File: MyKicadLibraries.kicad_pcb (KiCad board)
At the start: 2 copper layers, 168.6 x 98.9 mm, 32 parts, among them J1 Conn_01x08, J10 RCJ-22, J11 DIN-5, J12 Mini-DIN-6, J13 USB_A, J2 Conn_01x08, J3 POGO Pins, J4 c8-inlet, J5 FTDI, J6 Micro_SD_Card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

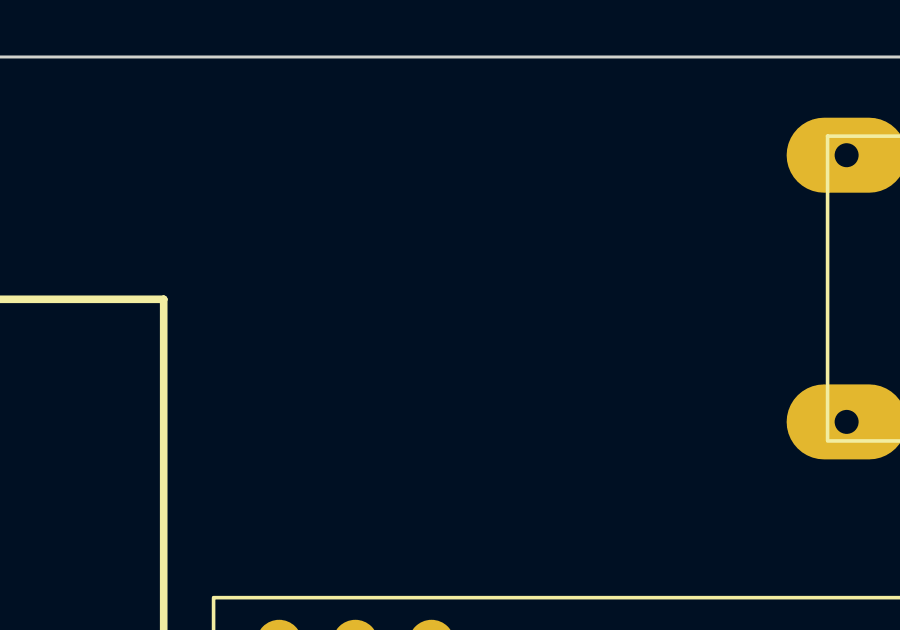
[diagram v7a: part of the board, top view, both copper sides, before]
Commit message: Add TCND5000 Library
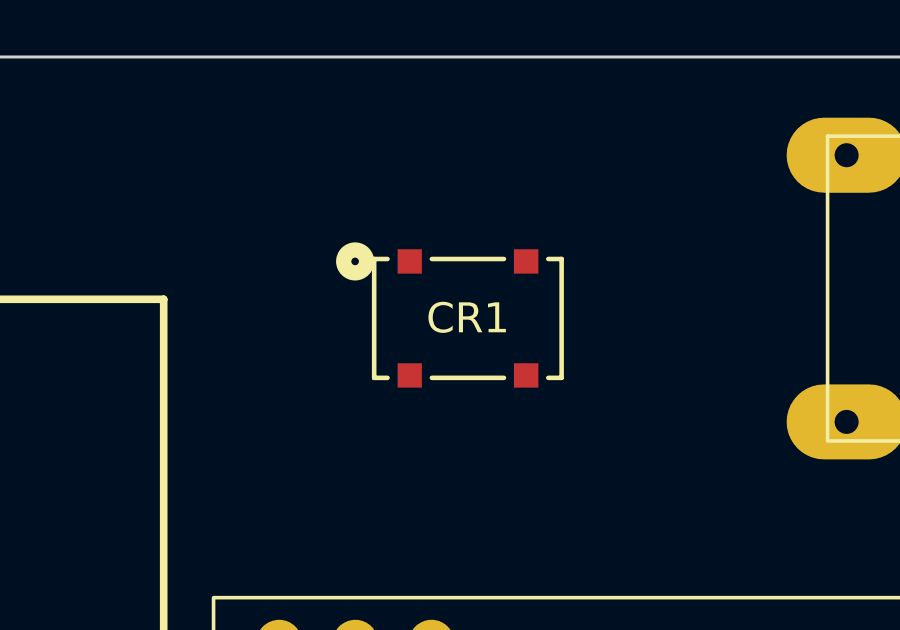
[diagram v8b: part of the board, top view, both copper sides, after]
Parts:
- added CR1: tcnd5000, tcnd5000:tcnd5000, F.Cu at (210.0, 33.0)
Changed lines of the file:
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@@
   (net 231 "unconnected-(J13-Pad3)")
   (net 232 "unconnected-(J13-Pad4)")
+  (net 233 "unconnected-(CR1-Pad1)")
+  (net 234 "unconnected-(CR1-Pad2)")
+  (net 235 "unconnected-(CR1-Pad4)")
+  (net 236 "unconnected-(CR1-Pad3)")
   (footprint "esp32-wemos-d1-mini:esp32-wemos-d1-mini" (layer "F.Cu")
     (at 118.11 138.43)
@@
     )
   )
+  (footprint "tcnd5000:tcnd5000" (layer "F.Cu")
+    (at 210 33)
+    (tags "tcnd5000 ")
+    (property "Sheetfile" "MyKicadLibraries.kicad_sch")
+    (property "Sheetname" "")
+    (attr smd)
+    (fp_text reference "CR1" (at 0 0 unlocked) (layer "F.SilkS")
+      (effects (font (size 1 1) (thickness 0.15)))
+    )
+    (fp_text value "tcnd5000" (at 0 0 unlocked) (layer "F.Fab")
+      (effects (font (size 1 1) (thickness 0.15)))
+    )
+    (fp_text user "${REFERENCE}" (at 0 0 unlocked) (layer "F.Fab")
+      (effects (font (size 1 1) (thickness 0.15)))
+    )
+    (fp_circle (center -3.7592 -1.9) (end -3.3782 -1.9) (layer "B.SilkS") (width 0.508) (fill none))
+    (fp_line (start -3.1242 -1.9812) (end -3.1242 1.9812) (layer "F.SilkS") (width 0.1524))
+    (fp_line (start -1.200861 1.9812) (end 1.200861 1.9812) (layer "F.SilkS") (width 0.1524))
+    (fp_line (start -2.679141 -1.9812) (end -3.1242 -1.9812) (layer "F.SilkS") (width 0.1524))
+    (fp_line (start 1.200861 -1.9812) (end -1.200861 -1.9812) (layer "F.SilkS") (width 0.1524))
+    (fp_line (start -3.1242 1.9812) (end -2.679141 1.9812) (layer "F.SilkS") (width 0.1524))
+    (fp_line (start 3.1242 -1.9812) (end 2.679141 -1.9812) (layer "F.SilkS") (width 0.1524))
+    (fp_line (start 2.679141 1.9812) (end 3.1242 1.9812) (layer "F.SilkS") (width 0.1524))
+    (fp_line (start 3.1242 1.9812) (end 3.1242 -1.9812) (layer "F.SilkS") (width 0.1524))
+    (fp_circle (center -3.7592 -1.9) (end -3.3782 -1.9) (layer "F.SilkS") (width 0.508) (fill none))
+    (fp_line (start 3.2512 -2.560399) (end -3.2512 -2.560399) (layer "F.CrtYd") (width 0.1524))
+    (fp_line (start 3.2512 2.560399) (end 3.2512 -2.560399) (layer "F.CrtYd") (width 0.1524))
+    (fp_line (start -3.2512 -2.560399) (end -3.2512 2.560399) (layer "F.CrtYd") (width 0.1524))
+    (fp_line (start -3.2512 2.560399) (end 3.2512 2.560399) (layer "F.CrtYd") (width 0.1524))
+    (fp_line (start 2.9972 -1.8542) (end -2.9972 -1.8542) (layer "F.Fab") (width 0.0254))
+    (fp_line (start 2.9972 1.8542) (end 2.9972 -1.8542) (layer "F.Fab") (width 0.0254))
+    (fp_line (start -2.9972 -1.8542) (end -2.9972 1.8542) (layer "F.Fab") (width 0.0254))
+    (fp_line (start -2.9972 1.8542) (end 2.9972 1.8542) (layer "F.Fab") (width 0.0254))
+    (fp_circle (center -1.94 -3.805) (end -1.559 -3.805) (layer "F.Fab") (width 0.508) (fill none))
+    (pad "1" smd rect (at -1.940001 -1.899999) (size 0.8128 0.8128) (layers "F.Cu" "F.Paste" "F.Mask")
+      (net 233 "unconnected-(CR1-Pad1)") (pintype "unspecified"))
+    (pad "2" smd rect (at -1.940001 1.899999) (size 0.8128 0.8128) (layers "F.Cu" "F.Paste" "F.Mask")
+      (net 234 "unconnected-(CR1-Pad2)") (pintype "unspecified"))
+    (pad "3" smd rect (at 1.940001 1.899999) (size 0.8128 0.8128) (layers "F.Cu" "F.Paste" "F.Mask")
+      (net 236 "unconnected-(CR1-Pad3)") (pintype "unspecified"))
+    (pad "4" smd rect (at 1.940001 -1.899999) (size 0.8128 0.8128) (layers "F.Cu" "F.Paste" "F.Mask")
+      (net 235 "unconnected-(CR1-Pad4)") (pintype "unspecified"))
+    (model "${KIPRJMOD}/lib/tcnd5000/tcnd5000.step"
+      (offset (xyz 2 0.3 6.75))
+      (scale (xyz 1 1 1))
+      (rotate (xyz -90 0 0))
+    )
+  )
